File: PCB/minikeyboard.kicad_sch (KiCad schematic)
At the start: 7 parts, among them SW1 SW_Push, SW2 SW_Push, SW3 SW_Push, SW4 SW_Push, U1 XIAO-RP2040-DIP

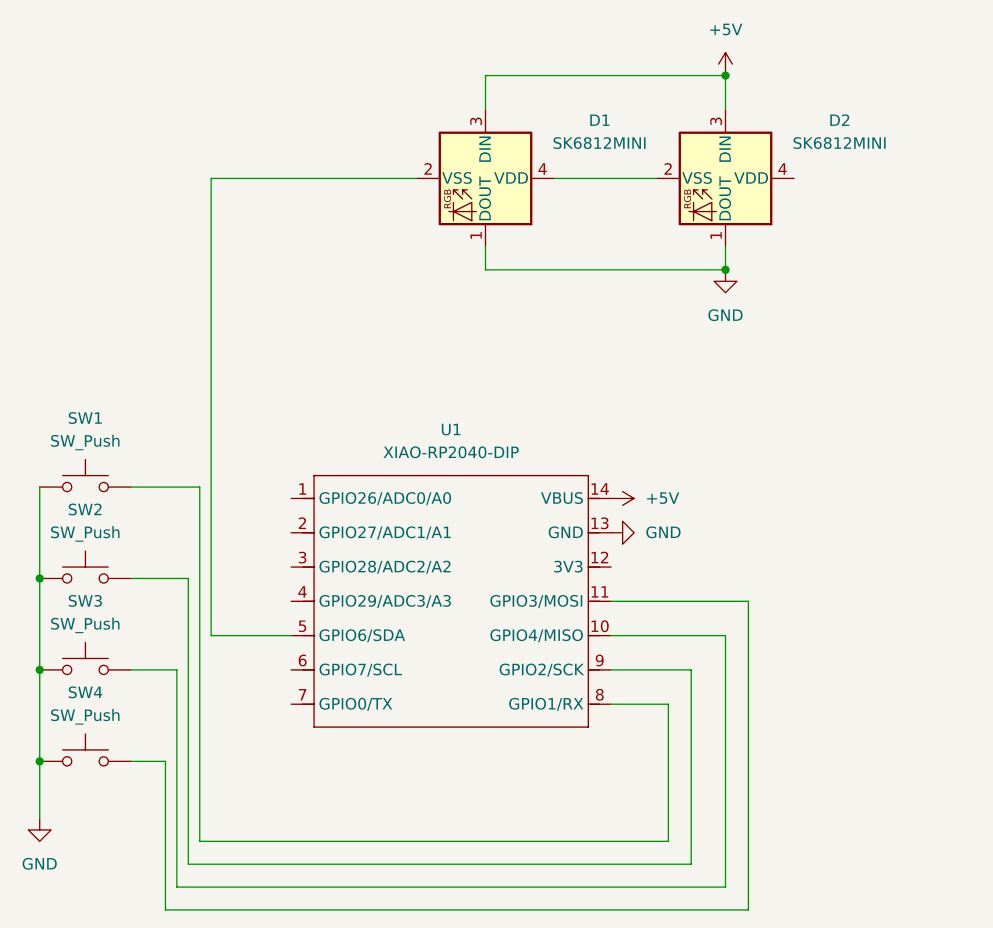
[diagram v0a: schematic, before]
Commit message: Change the code from QMK to KMK and added an encoder
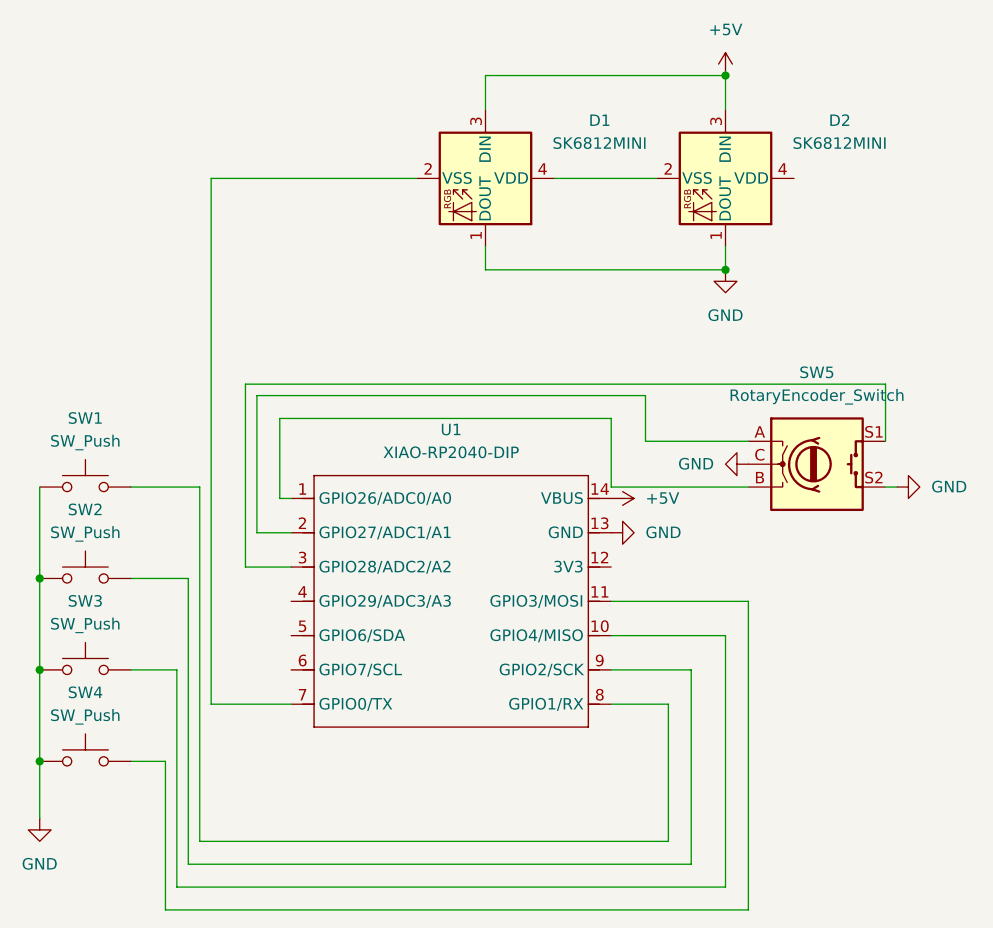
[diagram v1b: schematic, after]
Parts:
- added SW5: RotaryEncoder_Switch, Rotary_Encoder:RotaryEncoder_Alps_EC11E-Switch_Vertical_H20mm, symbol Device:RotaryEncoder_Switch
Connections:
- net GND: now also SW5.C, SW5.S2
- net at D1.2 (VSS): now also U1.7 (GPIO0/TX); no longer U1.5 (GPIO6/SDA)
- net at U1.1 (GPIO26/ADC0/A0): now also SW5.B
- net at U1.2 (GPIO27/ADC1/A1): now also SW5.A
- net at U1.3 (GPIO28/ADC2/A2): now also SW5.S1

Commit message: Add files via upload
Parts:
- D1, D2: footprint LED_SMD:LED_SK6812MINI_PLCC4_3.5x3.5mm_P1.75mm -> ledfoot:MX_SK6812MINI-E_REV
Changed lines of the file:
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@@
 			)
 		)
-		(property "Footprint" "LED_SMD:LED_SK6812MINI_PLCC4_3.5x3.5mm_P1.75mm"
+		(property "Footprint" "ledfoot:MX_SK6812MINI-E_REV"
 			(at 137.16 49.53 0)
 			(effects
@@
 			)
 		)
-		(property "Footprint" "LED_SMD:LED_SK6812MINI_PLCC4_3.5x3.5mm_P1.75mm"
+		(property "Footprint" "ledfoot:MX_SK6812MINI-E_REV"
 			(at 163.83 49.53 0)
 			(effects
